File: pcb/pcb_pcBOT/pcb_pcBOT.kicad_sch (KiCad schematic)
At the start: 0 parts

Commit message: fin bms schematic bms
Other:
- sheet bms ports: added I2C_SCL, INT_HOST, OTG_HOST, ~{CE}_HOST; removed none
- sheet stm32 ports: added I2C_SCL, I2C_SDA, MOT_AIN1, MOT_AIN2, MOT_BIN1, MOT_BIN2; removed none
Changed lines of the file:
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@@
 	)
 	(sheet
-		(at 30.48 148.59)
+		(at 22.86 133.35)
 		(size 66.04 40.64)
 		(exclude_from_sim no)
@@
 		)
 		(property "Sheetname" "capteur tof"
-			(at 30.48 147.8784 0)
+			(at 22.86 132.6384 0)
 			(effects
 				(font
@@
 		)
 		(property "Sheetfile" "tof.kicad_sch"
-			(at 30.48 189.8146 0)
+			(at 22.86 174.5746 0)
 			(effects
 				(font
@@
 	)
 	(sheet
-		(at 186.69 33.02)
+		(at 194.31 24.13)
 		(size 81.28 40.64)
 		(exclude_from_sim no)
@@
 		)
 		(property "Sheetname" "driver_motor"
-			(at 186.69 32.3084 0)
+			(at 194.31 23.4184 0)
 			(effects
 				(font
@@
 		)
 		(property "Sheetfile" "drv.kicad_sch"
-			(at 186.69 74.2446 0)
+			(at 194.31 65.3546 0)
 			(effects
 				(font
@@
 	)
 	(sheet
-		(at 106.68 20.32)
+		(at 24.13 77.47)
 		(size 64.77 43.18)
 		(exclude_from_sim no)
@@
 		)
 		(property "Sheetname" "centrale imu"
-			(at 106.68 19.6084 0)
+			(at 24.13 76.7584 0)
 			(effects
 				(font
@@
 		)
 		(property "Sheetfile" "imu.kicad_sch"
-			(at 106.68 64.0846 0)
+			(at 24.13 121.2346 0)
 			(effects
 				(font
@@
 	)
 	(sheet
-		(at 123.19 80.01)
-		(size 44.45 45.72)
+		(at 105.41 30.48)
+		(size 71.12 124.46)
 		(exclude_from_sim no)
 		(in_bom yes)
@@
 		)
 		(property "Sheetname" "stm32"
-			(at 123.19 79.2984 0)
+			(at 105.41 29.7684 0)
 			(effects
 				(font
@@
 		)
 		(property "Sheetfile" "stm32.kicad_sch"
-			(at 123.19 126.3146 0)
-			(effects
-				(font
-					(size 1.27 1.27)
-				)
-				(justify left top)
+			(at 105.41 155.5246 0)
+			(effects
+				(font
+					(size 1.27 1.27)
+				)
+				(justify left top)
+			)
+		)
+		(pin "I2C_SCL" bidirectional
+			(at 105.41 35.56 180)
+			(effects
+				(font
+					(size 1.27 1.27)
+				)
+				(justify left)
+			)
+		)
+		(pin "I2C_SDA" bidirectional
+			(at 105.41 38.1 180)
+			(effects
+				(font
+					(size 1.27 1.27)
+				)
+				(justify left)
+			)
+		)
+		(pin "MOT_AIN1" bidirectional
+			(at 176.53 41.91 0)
+			(effects
+				(font
+					(size 1.27 1.27)
+				)
+				(justify right)
+			)
+		)
+		(pin "MOT_AIN2" bidirectional
+			(at 176.53 44.45 0)
+			(effects
+				(font
+					(size 1.27 1.27)
+				)
+				(justify right)
+			)
+		)
+		(pin "MOT_BIN1" bidirectional
+			(at 176.53 50.8 0)
+			(effects
+				(font
+					(size 1.27 1.27)
+				)
+				(justify right)
+			)
+		)
+		(pin "MOT_BIN2" bidirectional
+			(at 176.53 53.34 0)
+			(effects
+				(font
+					(size 1.27 1.27)
+				)
+				(justify right)
 			)
 		)
@@
 	)
 	(sheet
-		(at 27.94 25.4)
-		(size 58.42 74.93)
+		(at 22.86 24.13)
+		(size 60.96 40.64)
 		(exclude_from_sim no)
 		(in_bom yes)
@@
 		)
 		(property "Sheetname" "bms"
-			(at 27.94 24.6884 0)
+			(at 22.86 23.4184 0)
 			(effects
 				(font
@@
 		)
 		(property "Sheetfile" "bms.kicad_sch"
-			(at 27.94 100.9146 0)
+			(at 22.86 65.3546 0)
 			(effects
 				(font
@@
 		)
 		(pin "I2C_SDA" bidirectional
-			(at 86.36 39.37 0)
-			(effects
-				(font
+			(at 83.82 38.1 0)
+			(effects
+				(font
+					(size 1.27 1.27)
+				)
+				(justify right)
+			)
+		)
+		(pin "I2C_SCL" bidirectional
+			(at 83.82 40.64 0)
+			(effects
+				(font
+					(size 1.27 1.27)
+				)
+				(justify right)
+			)
+		)
+		(pin "INT_HOST" output
+			(at 83.82 48.26 0)
+			(effects
+				(font
+					(size 1.27 1.27)
+				)
+				(justify right)
+			)
+		)
+		(pin "OTG_HOST" input
+			(at 83.82 50.8 0)
+			(effects
+				(font
+					(size 1.27 1.27)
+				)
+				(justify right)
+			)
+		)
+		(pin "~{CE}_HOST" input
+			(at 83.82 53.34 0)
+			(effects
+				(font

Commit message: avancement des schematics
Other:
- added sheet nrf24l01 (nrf.kicad_sch)
- sheet centrale imu ports: added I2C_SCL, I2C_SDA, IMU_INT1; removed none
- sheet driver_motor ports: added MOT_AIN1, MOT_AIN2, MOT_BIN1, MOT_BIN2; removed none
- sheet stm32 ports: added IMU_INT1, INT_HOST, OTG_HOST, ~{CE}_HOST; removed none
- company: (none) -> ENSEA G5
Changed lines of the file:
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@@
 		(title "schematic_PcBot_2026")
 		(rev "1.0")
-	)
-	(sheet
-		(at 22.86 133.35)
-		(size 66.04 40.64)
+		(company "ENSEA G5")
+	)
+	(sheet
+		(at 199.39 124.46)
+		(size 63.5 34.29)
+		(exclude_from_sim no)
+		(in_bom yes)
+		(on_board yes)
+		(dnp no)
+		(fields_autoplaced yes)
+		(stroke
+			(width 0.1524)
+			(type solid)
+		)
+		(fill
+			(color 0 0 0 0.0000)
+		)
+		(property "Sheetname" "nrf24l01"
+			(at 199.39 123.7484 0)
+			(effects
+				(font
+					(size 1.27 1.27)
+				)
+				(justify left bottom)
+			)
+		)
+		(property "Sheetfile" "nrf.kicad_sch"
+			(at 199.39 159.3346 0)
+			(effects
+				(font
+					(size 1.27 1.27)
+				)
+				(justify left top)
+			)
+		)
+		(instances
+			(project "pcb_pcBOT"
+				(path "/704e4da3-8ee7-458f-8a0f-3fc97e8dc2a6"
+					(page "8")
+				)
+			)
+		)
+	)
+	(sheet
+		(at 199.39 74.93)
+		(size 62.23 41.91)
 		(exclude_from_sim no)
 		(in_bom yes)
@@
 		)
 		(property "Sheetname" "capteur tof"
-			(at 22.86 132.6384 0)
+			(at 199.39 74.2184 0)
 			(effects
 				(font
@@
 		)
 		(property "Sheetfile" "tof.kicad_sch"
-			(at 22.86 174.5746 0)
+			(at 199.39 117.4246 0)
 			(effects
 				(font
@@
 	)
 	(sheet
-		(at 194.31 24.13)
-		(size 81.28 40.64)
+		(at 27.94 92.71)
+		(size 53.34 54.61)
 		(exclude_from_sim no)
 		(in_bom yes)
@@
 		)
 		(property "Sheetname" "driver_motor"
-			(at 194.31 23.4184 0)
+			(at 27.94 91.9984 0)
 			(effects
 				(font
@@
 		)
 		(property "Sheetfile" "drv.kicad_sch"
-			(at 194.31 65.3546 0)
-			(effects
-				(font
-					(size 1.27 1.27)
-				)
-				(justify left top)
+			(at 27.94 147.9046 0)
+			(effects
+				(font
+					(size 1.27 1.27)
+				)
+				(justify left top)
+			)
+		)
+		(pin "MOT_AIN1" input
+			(at 81.28 101.6 0)
+			(effects
+				(font
+					(size 1.27 1.27)
+				)
+				(justify right)
+			)
+		)
+		(pin "MOT_AIN2" input
+			(at 81.28 104.14 0)
+			(effects
+				(font
+					(size 1.27 1.27)
+				)
+				(justify right)
+			)
+		)
+		(pin "MOT_BIN1" input
+			(at 81.28 110.49 0)
+			(effects
+				(font
+					(size 1.27 1.27)
+				)
+				(justify right)
+			)
+		)
+		(pin "MOT_BIN2" input
+			(at 81.28 113.03 0)
+			(effects
+				(font
+					(size 1.27 1.27)
+				)
+				(justify right)
 			)
 		)
@@
 	)
 	(sheet
-		(at 24.13 77.47)
-		(size 64.77 43.18)
+		(at 199.39 24.13)
+		(size 60.96 41.91)
 		(exclude_from_sim no)
 		(in_bom yes)
@@
 		)
 		(property "Sheetname" "centrale imu"
-			(at 24.13 76.7584 0)
+			(at 199.39 23.4184 0)
 			(effects
 				(font
@@
 		)
 		(property "Sheetfile" "imu.kicad_sch"
-			(at 24.13 121.2346 0)
-			(effects
-				(font
-					(size 1.27 1.27)
-				)
-				(justify left top)
+			(at 199.39 66.6246 0)
+			(effects
+				(font
+					(size 1.27 1.27)
+				)
+				(justify left top)
+			)
+		)
+		(pin "I2C_SCL" bidirectional
+			(at 199.39 33.02 180)
+			(effects
+				(font
+					(size 1.27 1.27)
+				)
+				(justify left)
+			)
+		)
+		(pin "I2C_SDA" bidirectional
+			(at 199.39 35.56 180)
+			(effects
+				(font
+					(size 1.27 1.27)
+				)
+				(justify left)
+			)
+		)
+		(pin "IMU_INT1" output
+			(at 199.39 46.99 180)
+			(effects
+				(font
+					(size 1.27 1.27)
+				)
+				(justify left)
 			)
 		)
@@
 	)
 	(sheet
-		(at 105.41 30.48)
+		(at 106.68 27.94)
 		(size 71.12 124.46)
 		(exclude_from_sim no)
@@
 		)
 		(property "Sheetname" "stm32"
-			(at 105.41 29.7684 0)
+			(at 106.68 27.2284 0)
 			(effects
 				(font
@@
 		)
 		(property "Sheetfile" "stm32.kicad_sch"
-			(at 105.41 155.5246 0)
+			(at 106.68 152.9846 0)
 			(effects
 				(font
@@
 		)
 		(pin "I2C_SCL" bidirectional
-			(at 105.41 35.56 180)
+			(at 106.68 33.02 180)
 			(effects
 				(font
@@
 		)
 		(pin "I2C_SDA" bidirectional
-			(at 105.41 38.1 180)
+			(at 106.68 35.56 180)
 			(effects
 				(font
@@
 		)
 		(pin "MOT_AIN1" bidirectional
-			(at 176.53 41.91 0)
-			(effects
-				(font
-					(size 1.27 1.27)
-				)
-				(justify right)
+			(at 106.68 101.6 180)
+			(effects
+				(font
+					(size 1.27 1.27)
+				)
+				(justify left)
 			)
 		)
 		(pin "MOT_AIN2" bidirectional
-			(at 176.53 44.45 0)
-			(effects
-				(font
-					(size 1.27 1.27)
-				)
-				(justify right)
+			(at 106.68 104.14 180)
+			(effects
+				(font
+					(size 1.27 1.27)
+				)
+				(justify left)
 			)
 		)
 		(pin "MOT_BIN1" bidirectional
-			(at 176.53 50.8 0)
-			(effects
-				(font
-					(size 1.27 1.27)
-				)
-				(justify right)
+			(at 106.68 110.49 180)
+			(effects
+				(font
+					(size 1.27 1.27)
+				)
+				(justify left)
 			)
 		)
 		(pin "MOT_BIN2" bidirectional
-			(at 176.53 53.34 0)
-			(effects
-				(font
-					(size 1.27 1.27)
-				)
-				(justify right)
+			(at 106.68 113.03 180)
+			(effects
+				(font
+					(size 1.27 1.27)
+				)
+				(justify left)
+			)
+		)
+		(pin "IMU_INT1" input
+			(at 177.8 46.99 0)
+			(effects
+				(font
+					(size 1.27 1.27)
+				)
+				(justify right)
+			)
+		)
+		(pin "INT_HOST" input
+			(at 106.68 52.07 180)
+			(effects
+				(font
+					(size 1.27 1.27)
+				)
+				(justify left)
+			)
+		)
+		(pin "OTG_HOST" input
+			(at 106.68 54.61 180)
+			(effects
+				(font
+					(size 1.27 1.27)
+				)
+				(justify left)
+			)
+		)
+		(pin "~{CE}_HOST" input
+			(at 106.68 57.15 180)
+			(effects
+				(font
+					(size 1.27 1.27)
+				)
+				(justify left)
 			)
 		)
@@
 	)
 	(sheet
-		(at 22.86 24.13)
-		(size 60.96 40.64)
+		(at 27.94 27.94)
+		(size 49.53 48.26)
 		(exclude_from_sim no)
 		(in_bom yes)
@@
 		)
 		(property "Sheetname" "bms"
-			(at 22.86 23.4184 0)
+			(at 27.94 27.2284 0)
 			(effects
 				(font
@@
 		)
 		(property "Sheetfile" "bms.kicad_sch"
-			(at 22.86 65.3546 0)
+			(at 27.94 76.7846 0)
 			(effects
 				(font
@@
 		)
 		(pin "I2C_SDA" bidirectional
-			(at 83.82 38.1 0)
+			(at 77.47 31.75 0)
 			(effects
 				(font
@@
 		)
 		(pin "I2C_SCL" bidirectional
-			(at 83.82 40.64 0)
+			(at 77.47 34.29 0)
 			(effects
 				(font
@@
 		)
 		(pin "INT_HOST" output
-			(at 83.82 48.26 0)
+			(at 77.47 52.07 0)
 			(effects
 				(font
@@
 		)
 		(pin "OTG_HOST" input
-			(at 83.82 50.8 0)
+			(at 77.47 54.61 0)
 			(effects
 				(font
@@
 		)
 		(pin "~{CE}_HOST" input
-			(at 83.82 53.34 0)
-			(effects
-				(font
+			(at 77.47 57.15 0)
+			(effects
+				(font

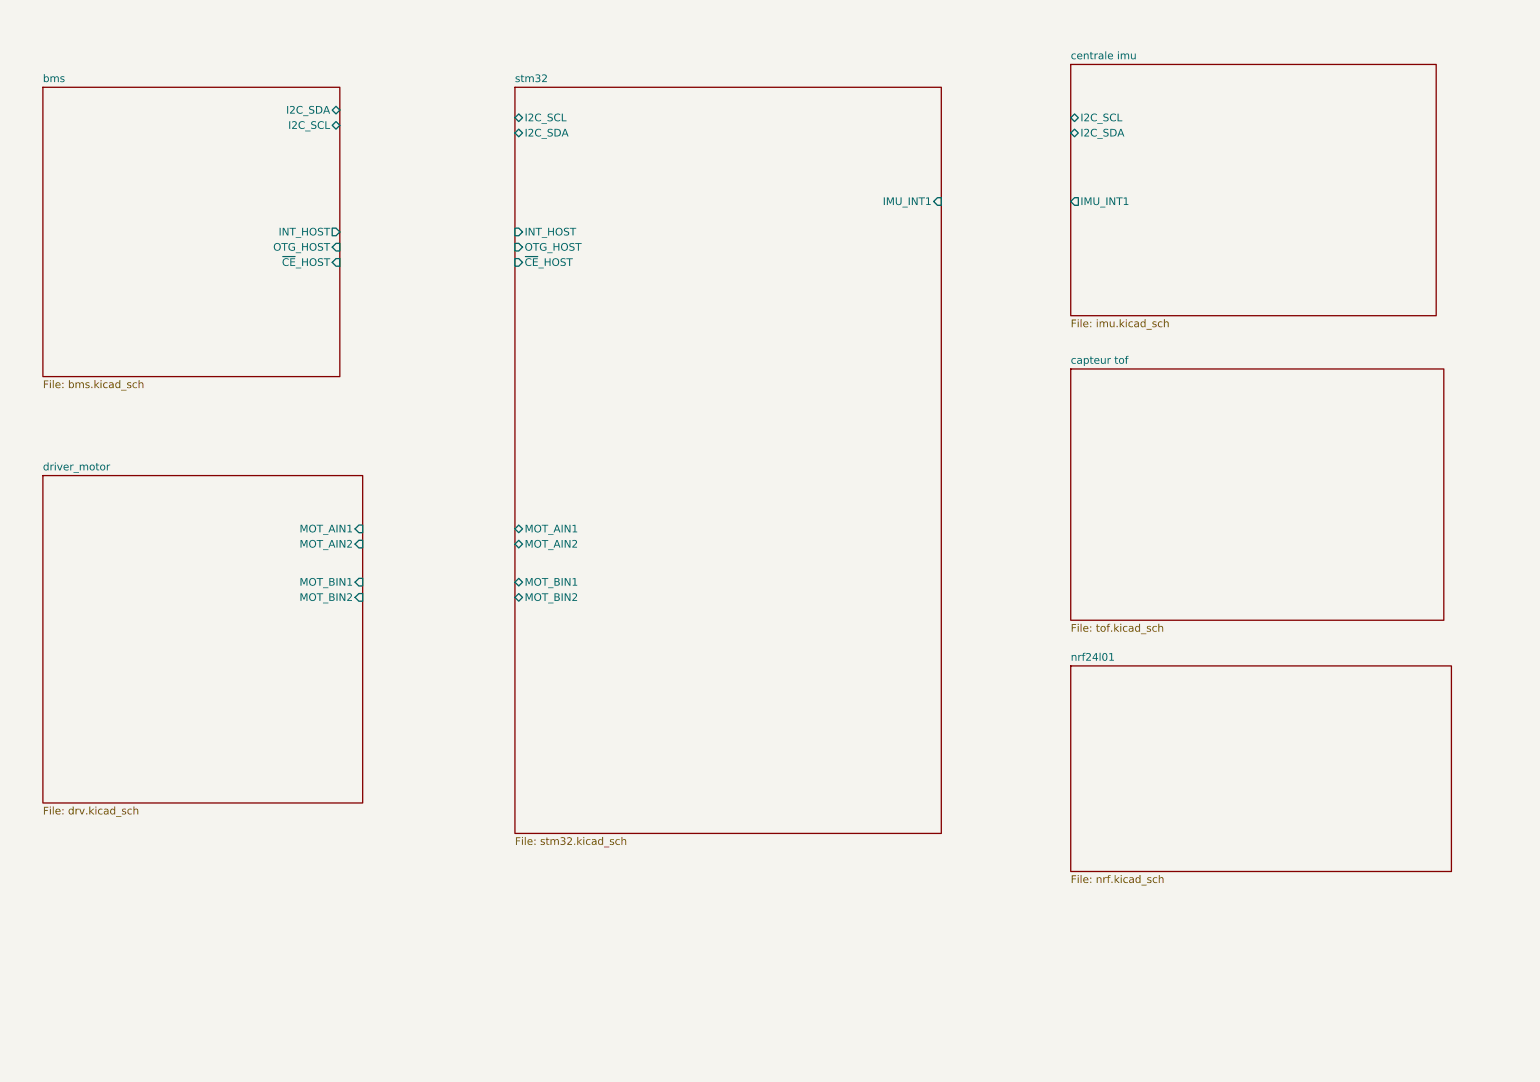
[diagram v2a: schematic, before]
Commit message: ajout du module nrf + petites corrections
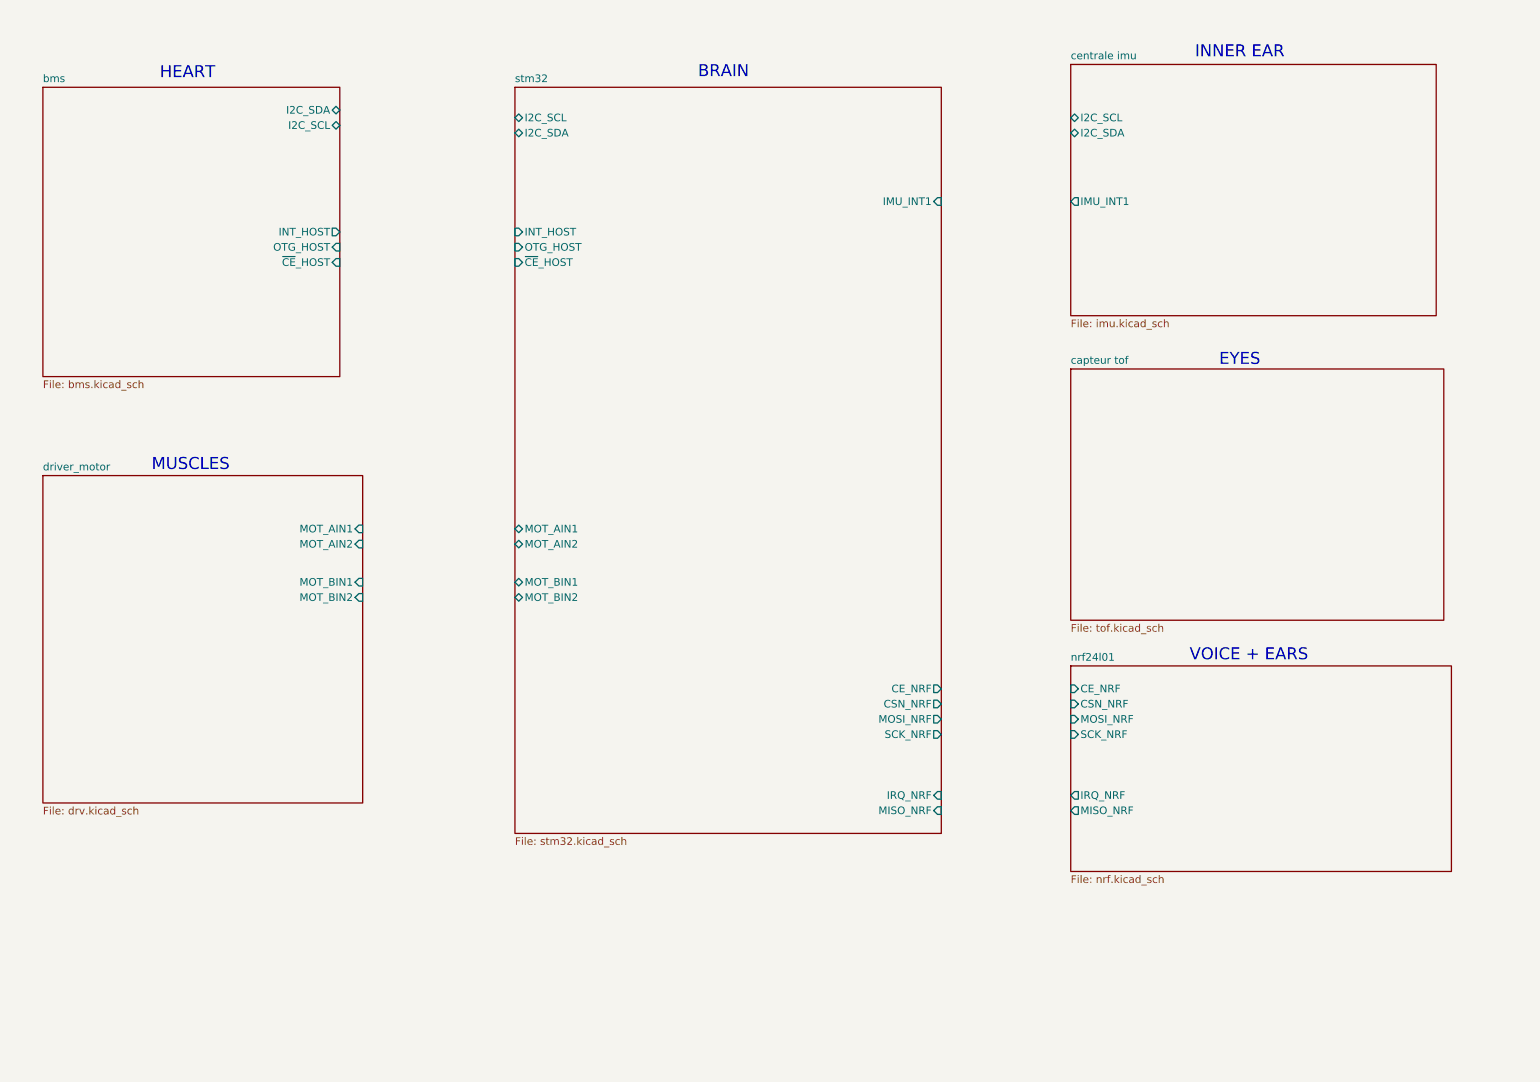
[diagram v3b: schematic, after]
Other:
- sheet nrf24l01 ports: added CE_NRF, CSN_NRF, IRQ_NRF, MISO_NRF, MOSI_NRF, SCK_NRF; removed none
- sheet stm32 ports: added CE_NRF, CSN_NRF, IRQ_NRF, MISO_NRF, MOSI_NRF, SCK_NRF; removed none
- note added: "BRAIN"
- note added: "EYES"
- note added: "HEART"
- note added: "INNER EAR"
- note added: "MUSCLES"
- note added: "VOICE + EARS"
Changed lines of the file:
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@@
 		(company "ENSEA G5")
+	)
+	(text "BRAIN"
+		(exclude_from_sim no)
+		(at 141.478 25.4 0)
+		(effects
+			(font
+				(size 2 2)
+			)
+		)
+	)
+	(text "EYES"
+		(exclude_from_sim no)
+		(at 227.584 73.406 0)
+		(effects
+			(font
+				(size 2 2)
+			)
+		)
+	)
+	(text "HEART\n\n"
+		(exclude_from_sim no)
+		(at 52.07 27.178 0)
+		(effects
+			(font
+				(size 2 2)
+			)
+		)
+	)
+	(text "VOICE + EARS\n"
+		(exclude_from_sim no)
+		(at 229.108 122.682 0)
+		(effects
+			(font
+				(size 2 2)
+			)
+		)
+	)
+	(text "INNER EAR\n"
+		(exclude_from_sim no)
+		(at 227.584 22.098 0)
+		(effects
+			(font
+				(size 2 2)
+			)
+		)
+	)
+	(text "MUSCLES"
+		(exclude_from_sim no)
+		(at 52.578 90.932 0)
+		(effects
+			(font
+				(size 2 2)
+			)
+		)
 	)
 	(sheet
@@
 			)
 		)
+		(pin "CE_NRF" input
+			(at 199.39 128.27 180)
+			(effects
+				(font
+					(size 1.27 1.27)
+				)
+				(justify left)
+			)
+		)
+		(pin "CSN_NRF" input
+			(at 199.39 130.81 180)
+			(effects
+				(font
+					(size 1.27 1.27)
+				)
+				(justify left)
+			)
+		)
+		(pin "IRQ_NRF" output
+			(at 199.39 146.05 180)
+			(effects
+				(font
+					(size 1.27 1.27)
+				)
+				(justify left)
+			)
+		)
+		(pin "MISO_NRF" output
+			(at 199.39 148.59 180)
+			(effects
+				(font
+					(size 1.27 1.27)
+				)
+				(justify left)
+			)
+		)
+		(pin "MOSI_NRF" input
+			(at 199.39 133.35 180)
+			(effects
+				(font
+					(size 1.27 1.27)
+				)
+				(justify left)
+			)
+		)
+		(pin "SCK_NRF" input
+			(at 199.39 135.89 180)
+			(effects
+				(font
+					(size 1.27 1.27)
+				)
+				(justify left)
+			)
+		)
 		(instances
 			(project "pcb_pcBOT"
@@
 			)
 		)
+		(pin "CE_NRF" output
+			(at 177.8 128.27 0)
+			(effects
+				(font
+					(size 1.27 1.27)
+				)
+				(justify right)
+			)
+		)
+		(pin "CSN_NRF" output
+			(at 177.8 130.81 0)
+			(effects
+				(font
+					(size 1.27 1.27)
+				)
+				(justify right)
+			)
+		)
+		(pin "IRQ_NRF" input
+			(at 177.8 146.05 0)
+			(effects
+				(font
+					(size 1.27 1.27)
+				)
+				(justify right)
+			)
+		)
+		(pin "MISO_NRF" input
+			(at 177.8 148.59 0)
+			(effects
+				(font
+					(size 1.27 1.27)
+				)
+				(justify right)
+			)
+		)
+		(pin "MOSI_NRF" output
+			(at 177.8 133.35 0)
+			(effects
+				(font
+					(size 1.27 1.27)
+				)
+				(justify right)
+			)
+		)
+		(pin "SCK_NRF" output
+			(at 177.8 135.89 0)
+			(effects
+				(font
+					(size 1.27 1.27)
+				)
+				(justify right)
+			)
+		)
